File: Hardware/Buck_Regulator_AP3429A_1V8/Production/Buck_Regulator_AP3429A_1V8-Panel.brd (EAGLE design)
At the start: 226.8 x 169.2 mm, 2502 parts, among them J1 Screw Terminal, J10 Breakout Headers, J100 Breakout Headers, J101 Screw Terminal, J102 POWER_JACKPOWER_JACK_SLOT_COM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, J103 Breakout Headers, J104 Screw Terminal, J105 POWER_JACKPOWER_JACK_SLOT_COM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, J106 Breakout Headers, J107 Screw Terminal, J108 POWER_JACKPOWER_JACK_SLOT_COM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, J109 Breakout Headers, J11 Screw Terminal, J110 Screw Terminal, J111 POWER_JACKPOWER_JACK_SLOT_COM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, J112 Breakout Headers, J113 Screw Terminal, J114 POWER_JACKPOWER_JACK_SLOT_COM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, J115 Breakout Headers, J116 Screw Terminal, J117 POWER_JACKPOWER_JACK_SLOT_COM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, J118 Breakout Headers, J119 Screw Terminal, J12 POWER_JACKPOWER_JACK_SLOT_COM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, J120 POWER_JACKPOWER_JACK_SLOT_COM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, J121 Breakout Headers, J122 Screw Terminal, J123 POWER_JACKPOWER_JACK_SLOT_COM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, J124 Breakout Headers, J125 Screw Terminal, J126 POWER_JACKPOWER_JACK_SLOT_COM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, J127 Breakout Headers, J128 Screw Terminal, J129 POWER_JACKPOWER_JACK_SLOT_COM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, J13 Breakout Headers, J130 Breakout Headers, J131 Screw Terminal, J132 POWER_JACKPOWER_JACK_SLOT_COM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, J133 Breakout Headers, J134 Screw Terminal, J135 POWER_JACKPOWER_JACK_SLOT_COM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, J136 Breakout Headers, J137 Screw Terminal, J138 POWER_JACKPOWER_JACK_SLOT_COM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, J139 Breakout Headers, J14 Screw Terminal, J140 Screw Terminal, J141 POWER_JACKPOWER_JACK_SLOT_COM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, J142 Breakout Headers, J143 Screw Terminal, J144 POWER_JACKPOWER_JACK_SLOT_COM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, J15 POWER_JACKPOWER_JACK_SLOT_COM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, J16 Breakout Headers, J17 Screw Terminal, J18 POWER_JACKPOWER_JACK_SLOT_COM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, J19 Breakout Headers, J2 POWER_JACKPOWER_JACK_SLOT_COM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, J20 Screw Terminal, J21 POWER_JACKPOWER_JACK_SLOT_COM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, J22 Breakout Headers, J23 Screw Terminal, J24 POWER_JACKPOWER_JACK_SLOT_COM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, J25 Breakout Headers, J26 Screw Terminal, J27 POWER_JACKPOWER_JACK_SLOT_COM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, J28 Breakout Headers, J29 Screw Terminal, J3 Breakout Headers, J30 POWER_JACKPOWER_JACK_SLOT_COM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, J31 Breakout Headers, J32 Screw Terminal, J33 POWER_JACKPOWER_JACK_SLOT_COM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, J34 Breakout Headers, J35 Screw Terminal, J36 POWER_JACKPOWER_JACK_SLOT_COM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, J37 Breakout Headers, J38 Screw Terminal, J39 POWER_JACKPOWER_JACK_SLOT_COM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, J4 Breakout Headers, J40 Breakout Headers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

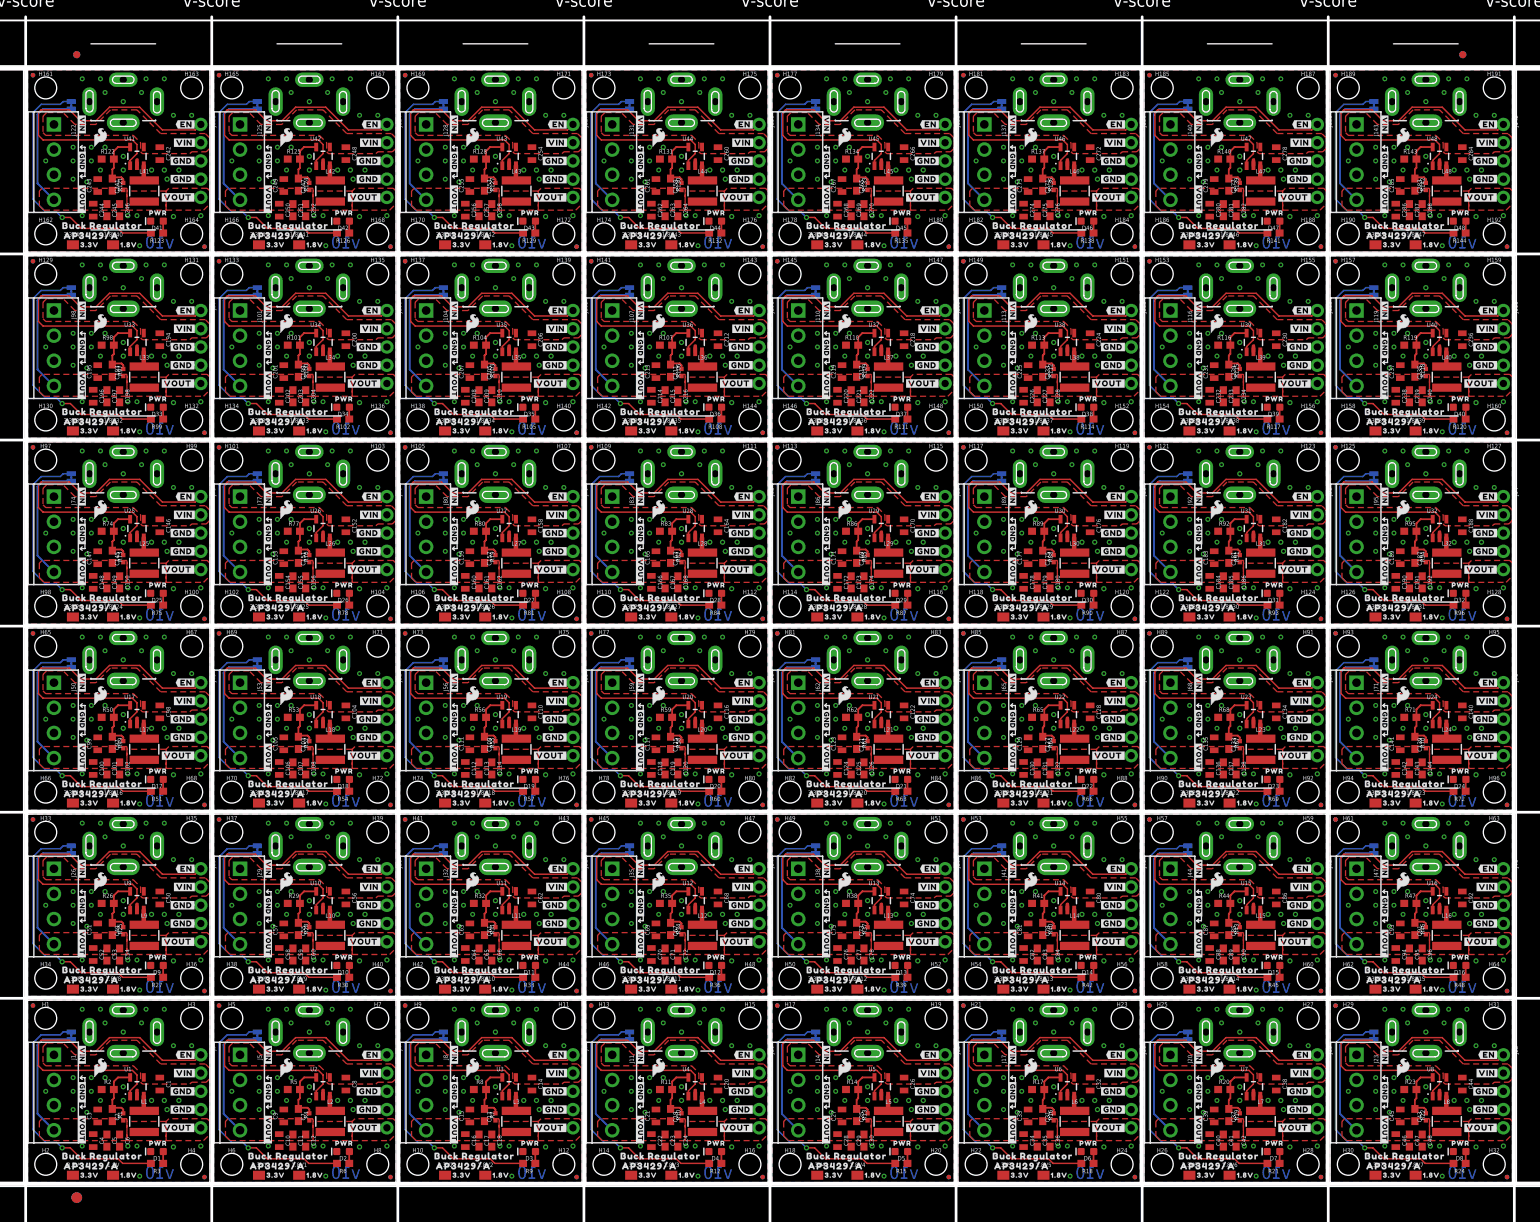
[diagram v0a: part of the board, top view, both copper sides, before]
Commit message: Adjusted power jack for panelizing
There was an issue with overhanging silkscreen for the powerjack since the part is usually populated - the part is not populated for this specific part. This was changed from the device all the way through the panelized files.
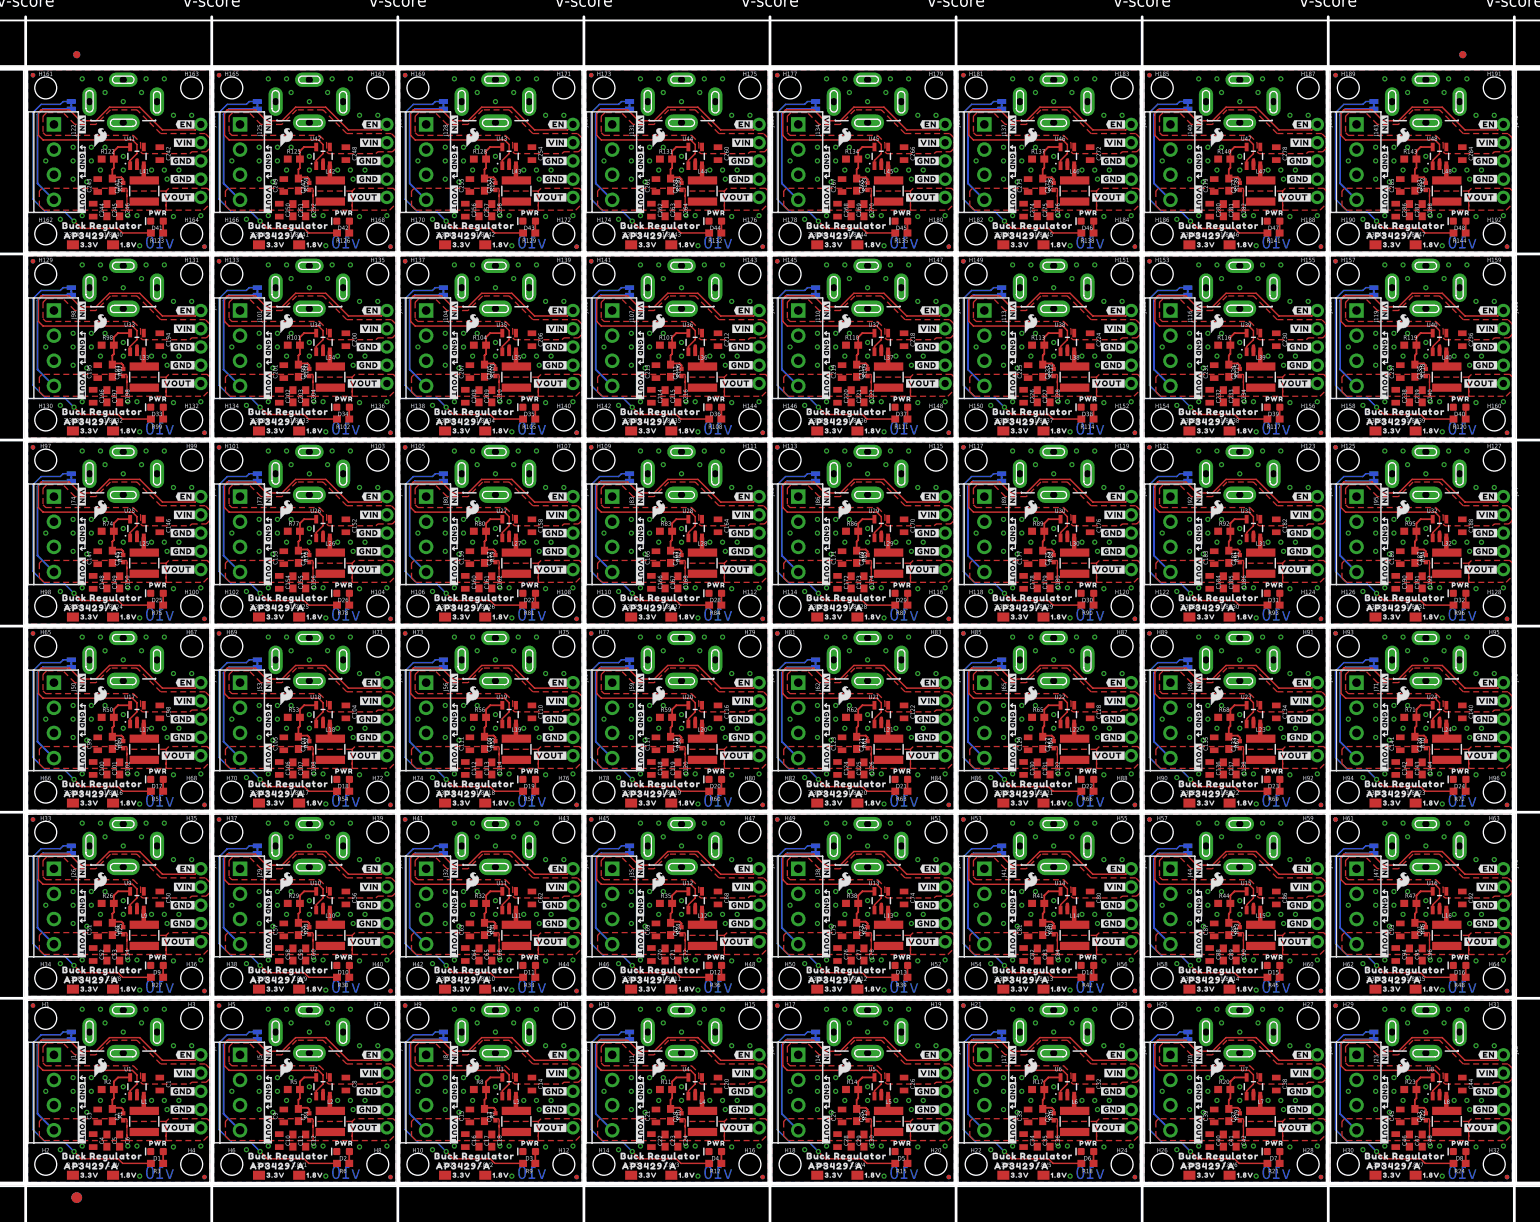
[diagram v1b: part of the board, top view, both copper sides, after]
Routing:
- net GND9: vias 30 -> 31
- net GND8: vias 30 -> 31
- net GND7: vias 30 -> 31
- net GND6: vias 30 -> 31
- net GND5: vias 30 -> 31
- net GND47: vias 30 -> 31
- net GND46: vias 30 -> 31
- net GND45: vias 30 -> 31
- net GND44: vias 30 -> 31
- net GND43: vias 30 -> 31
- net GND42: vias 30 -> 31
- net GND41: vias 30 -> 31
- net GND40: vias 30 -> 31
- net GND4: vias 30 -> 31
- net GND39: vias 30 -> 31
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
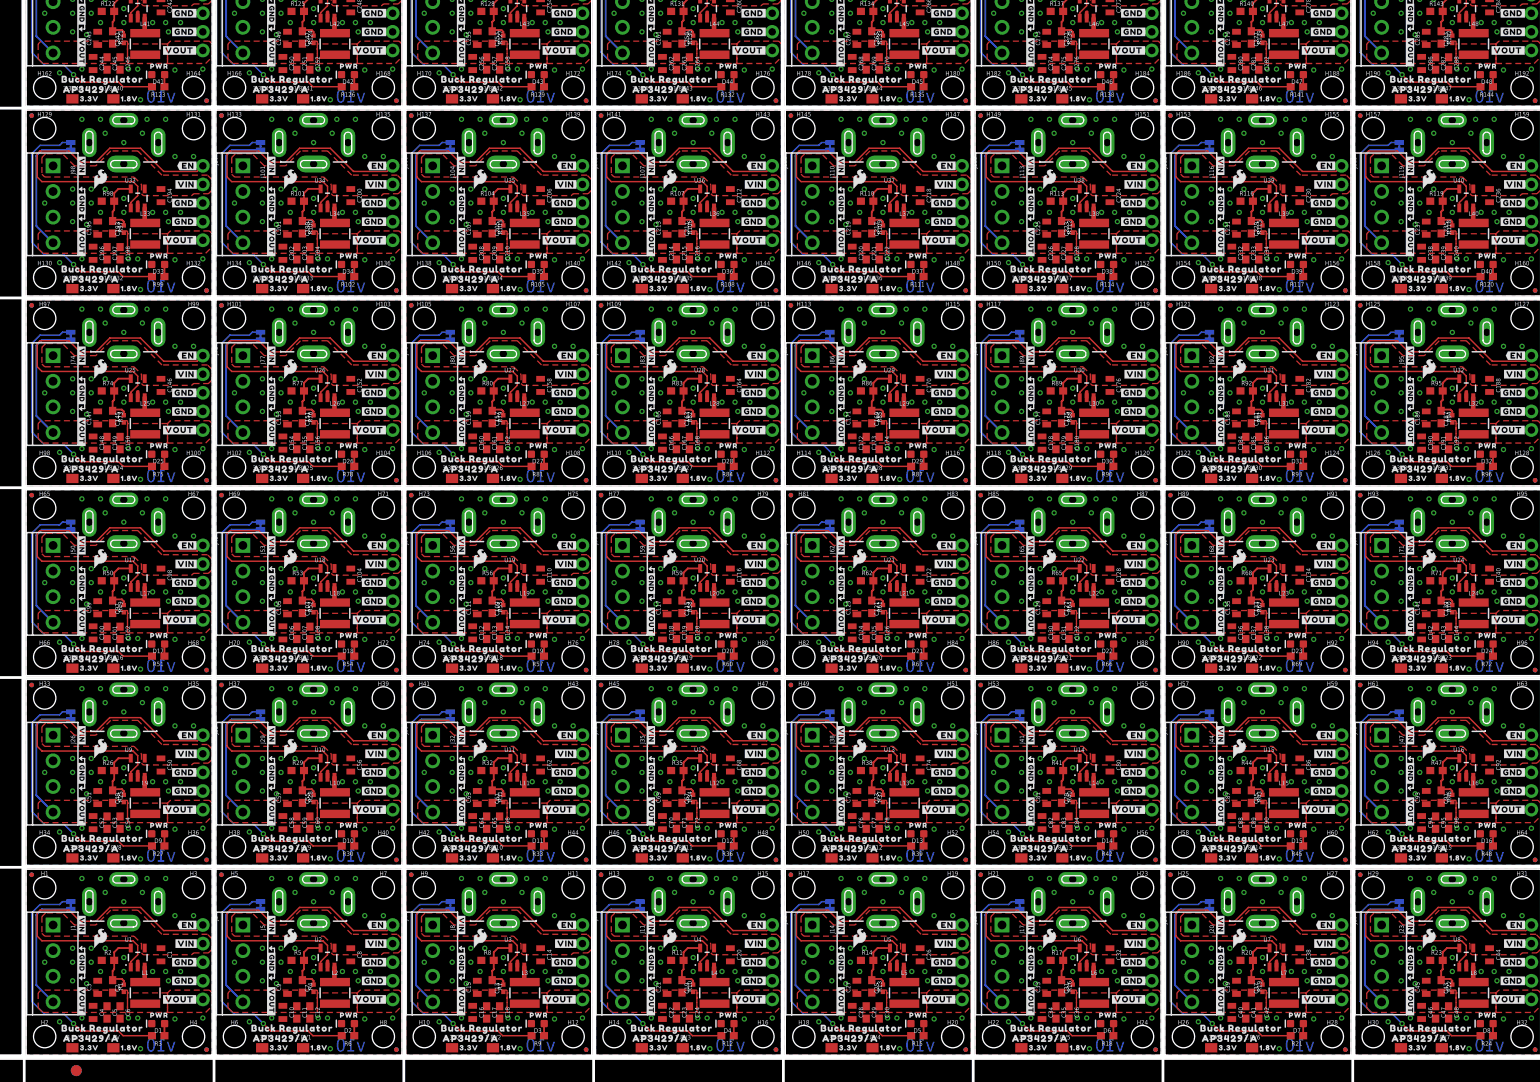
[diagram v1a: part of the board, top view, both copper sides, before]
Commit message: Updated panelized files
Adjusted via to no longer be in the way of the bStop on the back for the thermal pad on the backside. Included ordering instructions on the brd files for both 1.8V and 3.3V
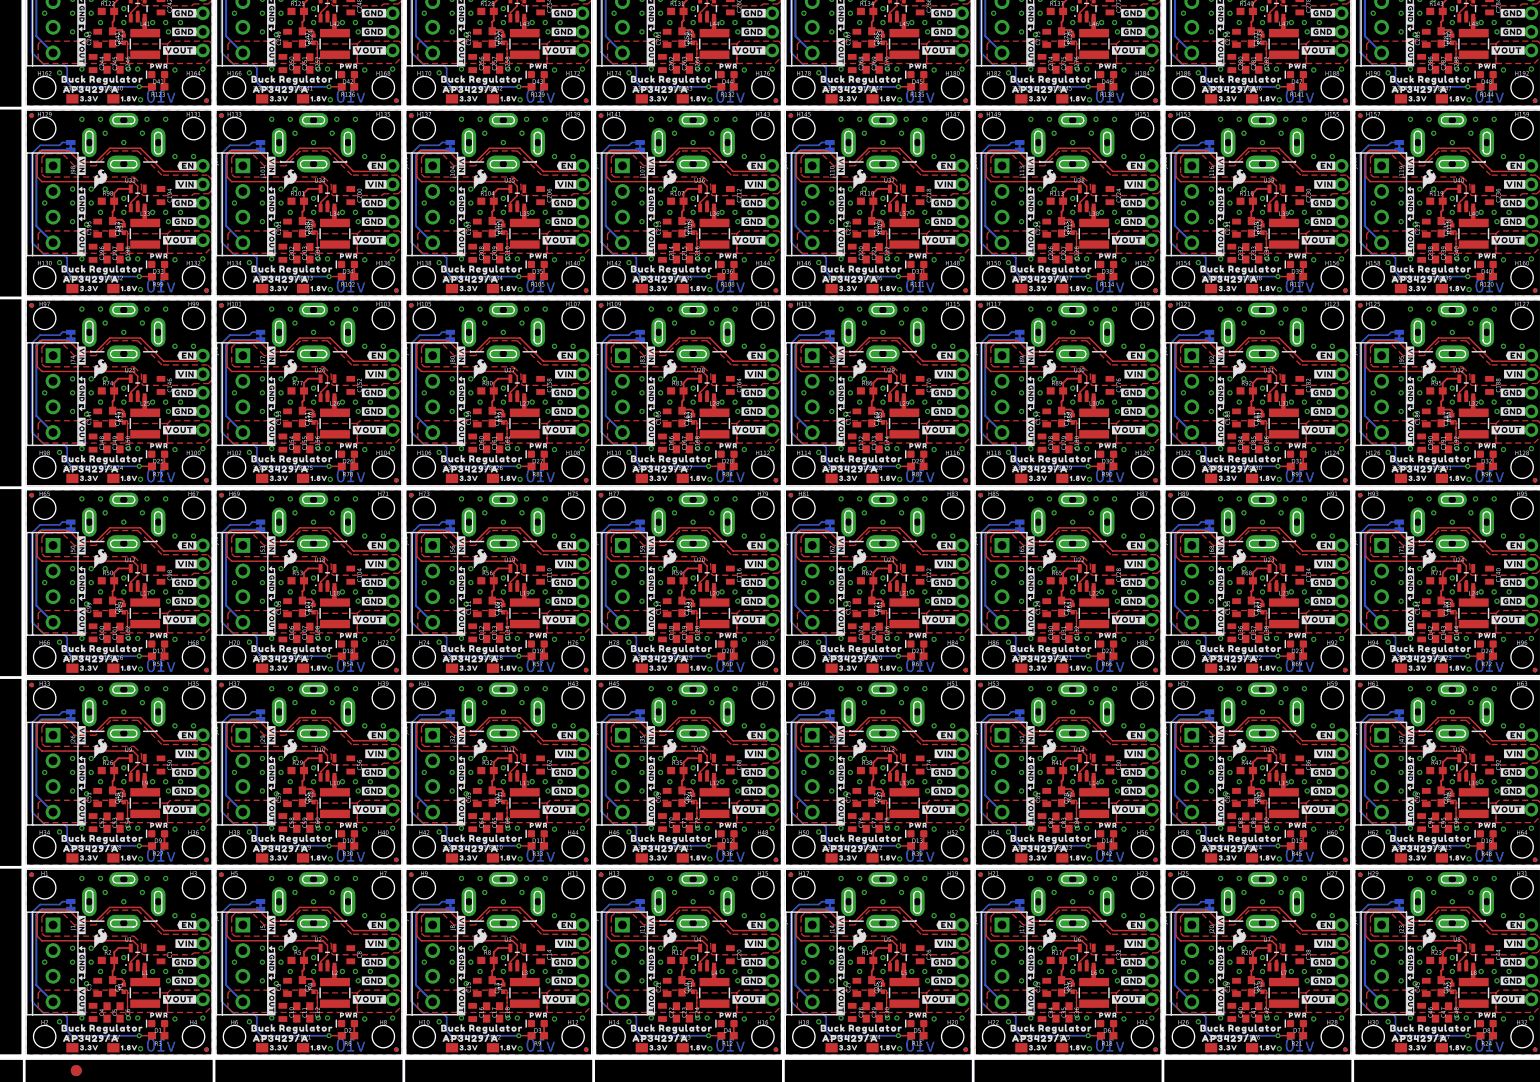
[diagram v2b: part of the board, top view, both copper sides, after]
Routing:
- net N$19: track 36.4 -> 37.5 mm
- net N$91: track 36.4 -> 37.5 mm
- net N$79: track 36.4 -> 37.5 mm
- net N$71: track 36.4 -> 37.5 mm
- net N$67: track 36.4 -> 37.5 mm
- net N$63: track 36.4 -> 37.5 mm
- net N$59: track 36.4 -> 37.5 mm
- net N$55: track 36.4 -> 37.5 mm
- net N$51: track 36.4 -> 37.5 mm
- net N$47: track 36.4 -> 37.5 mm
- net N$43: track 36.4 -> 37.5 mm
- net N$35: track 36.4 -> 37.5 mm
- net N$31: track 36.4 -> 37.5 mm
- net N$3: track 36.4 -> 37.5 mm
- net N$27: track 36.4 -> 37.5 mm
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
